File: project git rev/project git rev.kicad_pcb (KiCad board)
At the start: 2 copper layers, 94.8 x 45.2 mm, 31 parts, among them J1 Conn_01x03, J11 Conn_01x02, J4 Conn_01x02, J7 Conn_01x02, U1 LM358

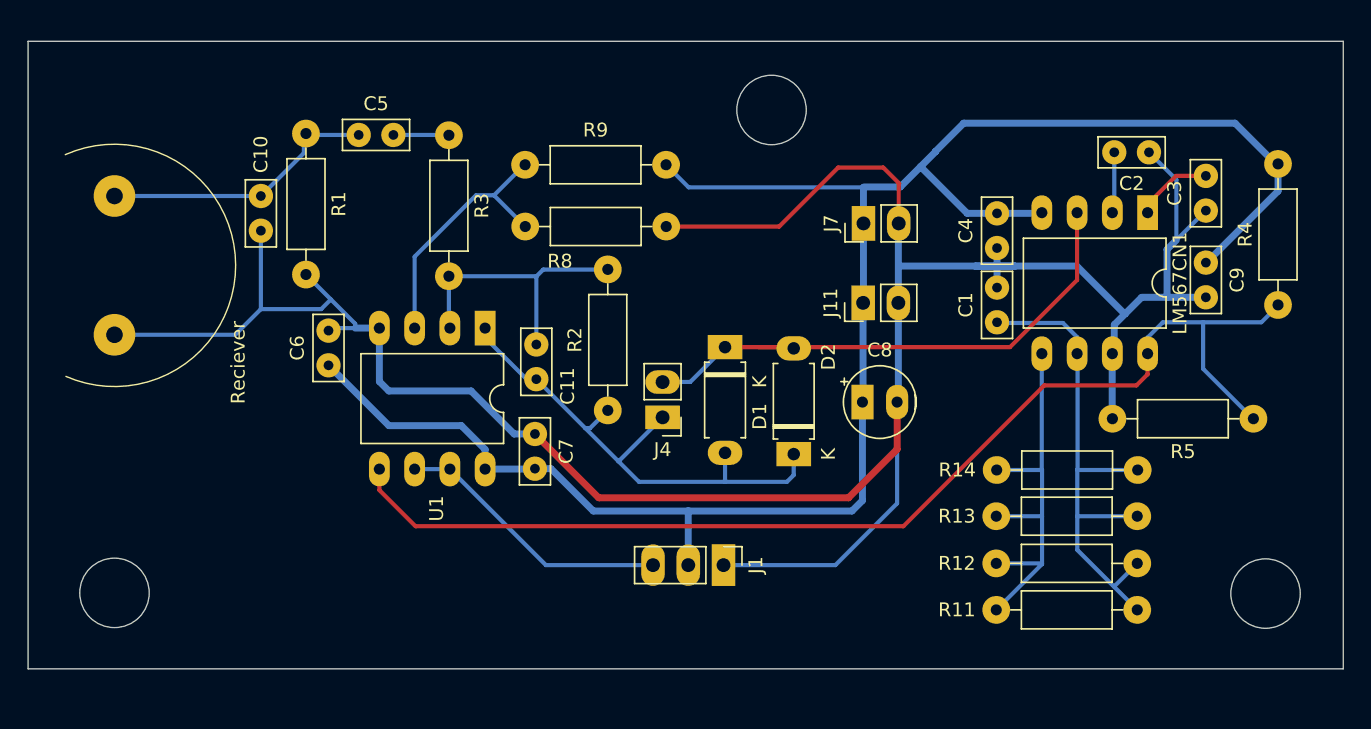
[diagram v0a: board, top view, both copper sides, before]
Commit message: Noen estetiske endringer + satt kanten og hull til milimeter grid
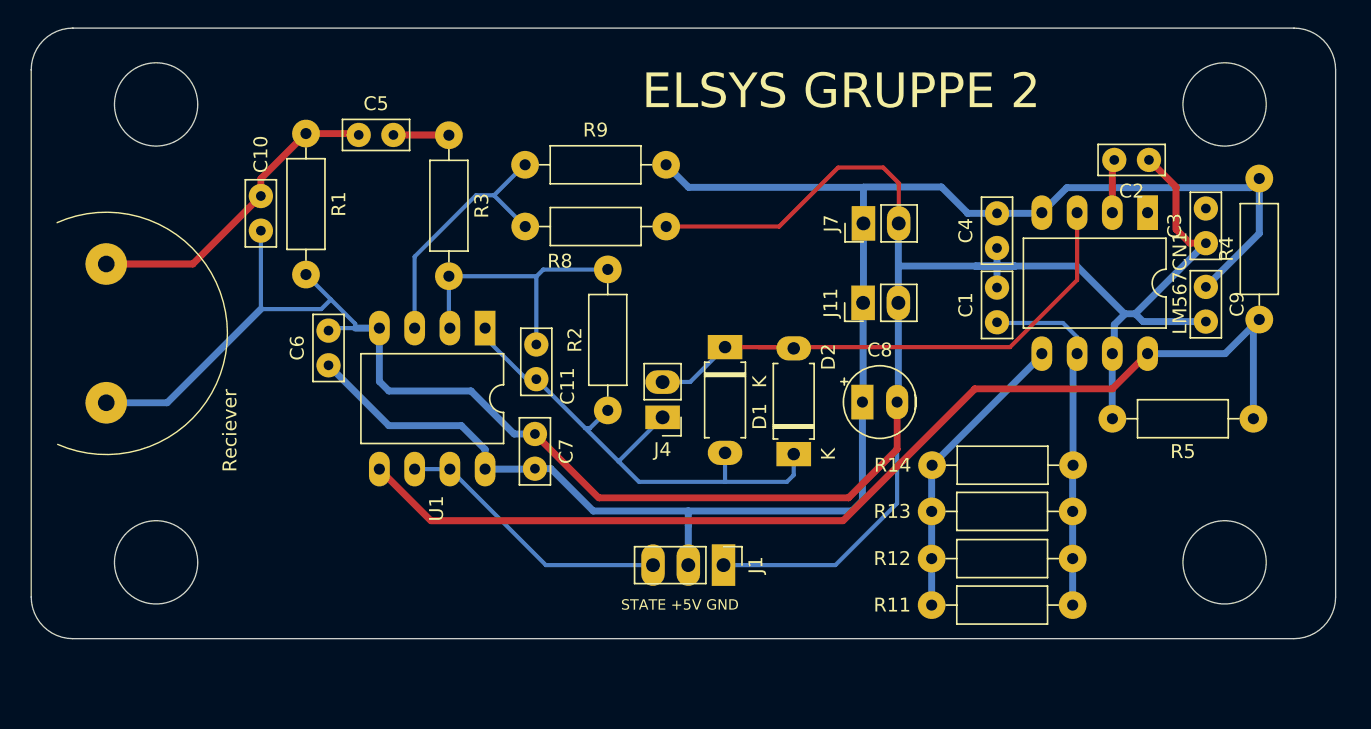
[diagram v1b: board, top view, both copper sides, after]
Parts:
- moved MK1 4.94 mm to (115.4, 103.5)
- moved R11 4.67 mm to (185.1, 118.1)
- moved R12 4.67 mm to (185.1, 114.7)
- moved R13 4.67 mm to (185.1, 111.3)
- moved R14 4.67 mm to (185.1, 108.0)
- moved C3 2.35 mm to (194.7, 92.0)
- moved C9 1.75 mm to (194.7, 95.2)
- moved R4 1.71 mm to (198.5, 97.5)
- moved C2 0.55 mm to (190.6, 86.0)
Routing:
- net Net-(LM567CN1-Timing_Capacitor): track 38.7 -> 25.7 mm
- net +5V: track 137.9 -> 125.2 mm
- net Net-(LM567CN1-Timing_Resistor): track 29.8 -> 21.4 mm
- net Net-(LM567CN1-Output): track 84.0 -> 78.3 mm
- net Net-(LM567CN1-Output_Filter): track 6.42 -> 1.72 mm
- net GND: track 190.3 -> 193.7 mm
- net Net-(MK1-+): track 20.2 -> 23.2 mm
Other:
- board size 94.8 x 45.2 mm -> 94 x 44 mm
- board text added: "ELSYS GRUPPE 2"
- board text added: "STATE +5V GND"

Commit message: Endret rutinger slik at referansepunkt ble like for deler av elektronikken (GND/5V) Endret unødvendig tykke ruter til tynne Endret rutene mellom de to strømtilkoblingene til å være 1 mm tykke Forminket antall koblinger til loddepunkt (for mindre varmeoverføringsevne til resten av kretsen => enklere å lodde)
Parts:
- moved R11 3.92 mm to (187.8, 115.3)
- moved R12 3.92 mm to (187.8, 112.0)
- moved R13 3.92 mm to (187.8, 108.6)
- moved R14 3.92 mm to (187.9, 105.2)
- moved R5 3.02 mm to (200.8, 103.3)
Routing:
- net +5V: track 125.2 -> 137.3 mm
- net GND: track 193.7 -> 198.4 mm
- net Net-(LM567CN1-Output_Filter): track 1.72 -> 5.62 mm
- net Net-(LM567CN1-Timing_Resistor): track 21.4 -> 17.6 mm
- net Net-(LM567CN1-Timing_Capacitor): track 25.7 -> 24.0 mm
- net Net-(LM567CN1-Output): track 78.3 -> 79.1 mm
- net Net-(U1A-+): track 19.0 -> 18.3 mm

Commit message: La til MCP adcen i kretsen og bestilte 👍
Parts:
- added C12: 10n, UR:C_Rect_L4.6mm_W2.0mm_P2.50mm_MKS02_FKP02, F.Cu at (182.5, 86.0)
- added C13: C, UR:C_Rect_L4.6mm_W2.0mm_P2.50mm_MKS02_FKP02, F.Cu at (144.4, 121.5)
- added C14: 100n, UR:C_Rect_L4.6mm_W2.0mm_P2.50mm_MKS02_FKP02, F.Cu at (151.4, 116.0)
- added C15: 1u, UR:C_Rect_L4.6mm_W2.0mm_P2.50mm_MKS02_FKP02, F.Cu at (141.9, 118.5)
- added C16: 10u, UR:C_Rect_L4.6mm_W2.0mm_P2.50mm_MKS02_FKP02, F.Cu at (147.4, 116.0)
- added J2: Conn_01x03_Pin, Connector_PinHeader_2.54mm:PinHeader_1x03_P2.54mm_Vertical, F.Cu at (152.9, 121.5)
- added J3: 3.3V input, Connector_PinHeader_2.54mm:PinHeader_1x01_P2.54mm_Vertical, F.Cu at (161.4, 116.0)
- added JP1: SolderJumper_3_Open, Jumper:SolderJumper-3_P2.0mm_Open_TrianglePad1.0x1.5mm, F.Cu at (155.9, 116.0)
- added R10: 5625, UR:R_Axial_DIN0207_L6.3mm_D2.5mm_P10.16mm_Horizontal, F.Cu at (138.9, 118.5)
- added R6: R, UR:R_Axial_DIN0207_L6.3mm_D2.5mm_P10.16mm_Horizontal, F.Cu at (128.8, 122.0)
- added R7: 10k, UR:R_Axial_DIN0207_L6.3mm_D2.5mm_P10.16mm_Horizontal, F.Cu at (144.4, 115.0)
- added U2: ~, Package_DFN_QFN:TDFN-10-1EP_2x3mm_P0.5mm_EP0.9x2mm, F.Cu at (149.0, 119.5)
- moved J1 11.6 mm to (171.5, 115.0)
- moved MK1 2.25 mm to (115.4, 105.8)
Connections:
- net Net-(D1-A) renamed MIC
- LM567CN1 pad 3: Signal -> Net-(LM567CN1-Signal)
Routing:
- net GND: track 198.4 -> 255.7 mm
- net +5V: track 137.3 -> 179.2 mm
- net MIC: track 38.0 -> 69.2 mm
- net Net-(U2-AVdd): track 0.00 -> 13.7 mm
- net State: track 20.0 -> 31.6 mm
- net Net-(U2-Ain+): track 0.00 -> 10.8 mm
- net Net-(JP1-C): track 0.00 -> 9.97 mm
- net Net-(J2-Pin_3): track 0.00 -> 8.86 mm
- net Net-(J2-Pin_2): track 0.00 -> 6.11 mm
- net Net-(LM567CN1-Signal): track 0.00 -> 5.38 mm
- net Net-(J3-Pin_1): track 0.00 -> 3.50 mm
- net Net-(J2-Pin_1): track 0.00 -> 3.36 mm
- net Net-(MK1-+): track 23.2 -> 24.1 mm
- net Net-(LM567CN1-Output): track 79.1 -> 78.3 mm
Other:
- board size 94 x 44 mm -> 93 x 48.5 mm
- board text added: "3v3"
- board text added: "CNVST SDO SCLK"
- board text added: "IGNORER, det er +5V COMMON +3V"
